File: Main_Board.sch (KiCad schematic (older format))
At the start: 64 parts, among them J1 DAC_12-bits, J2 Bias_Header, J3 Measurement_Header, Q1 Q_PNP_BCE, Q2 Q_NPN_BCE, U1 AD667, U2 LF356, U3 AD558JN

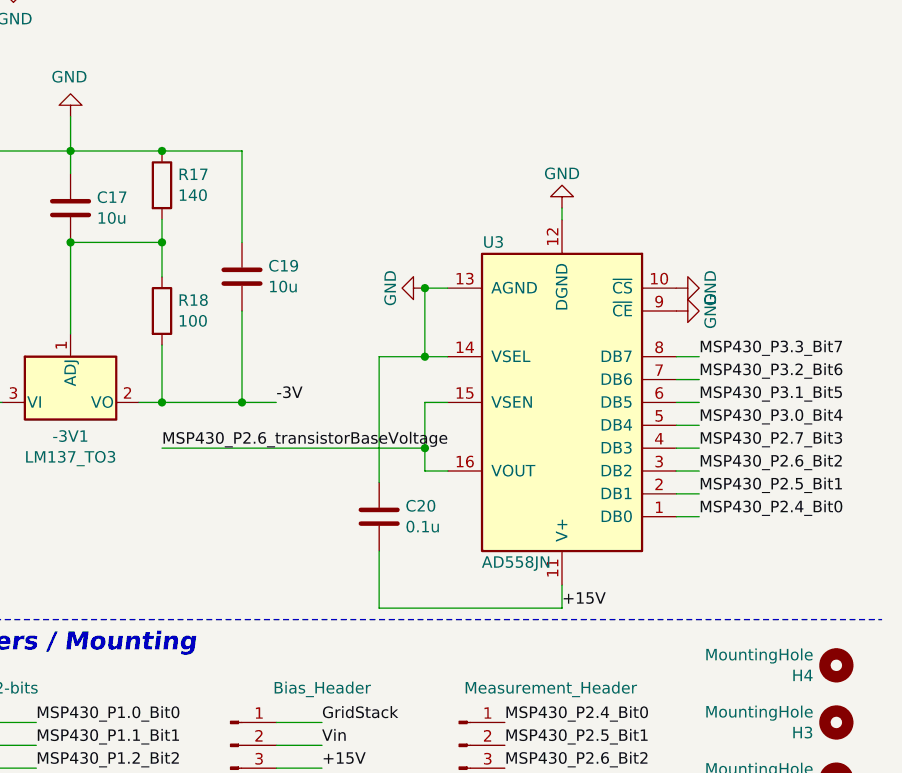
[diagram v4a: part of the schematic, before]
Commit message: Got rid of 8-bit DAC
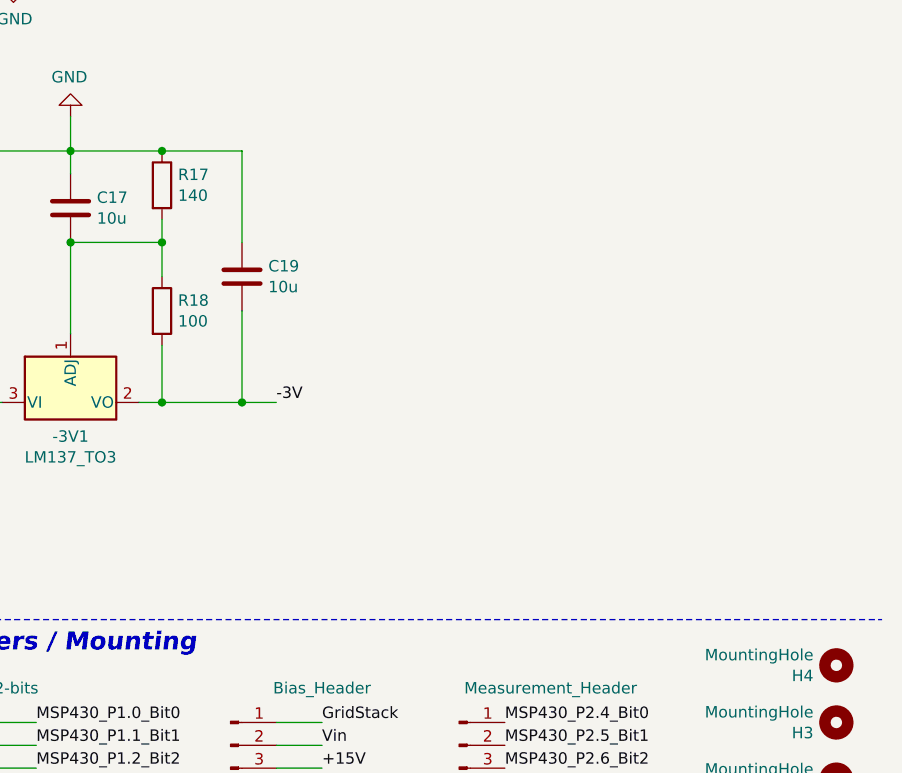
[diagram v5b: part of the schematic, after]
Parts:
- removed C20: 0.1u, Capacitor_SMD:C_0805_2012Metric, symbol Device:C
- removed U3: AD558JN, Package_DIP:DIP-16_W7.62mm_Socket, symbol Analog_DAC:AD558JN
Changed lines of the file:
@@
 	8000 1800 8000 1750
 Connection ~ 8000 1750
-Text Label 10450 3700 0    50   ~ 0
-MSP430_P3.3_Bit7
-Text Label 10450 3800 0    50   ~ 0
-MSP430_P3.2_Bit6
-Text Label 10450 3900 0    50   ~ 0
-MSP430_P3.1_Bit5
-Text Label 10450 4000 0    50   ~ 0
-MSP430_P3.0_Bit4
-Text Label 10450 4100 0    50   ~ 0
-MSP430_P2.7_Bit3
-Text Label 10450 4200 0    50   ~ 0
-MSP430_P2.6_Bit2
-Text Label 10450 4300 0    50   ~ 0
-MSP430_P2.5_Bit1
-Text Label 10450 4400 0    50   ~ 0
-MSP430_P2.4_Bit0
-Wire Wire Line
-	9850 3100 9850 3050
-Wire Wire Line
-	9850 4700 9850 4800
-Wire Wire Line
-	9350 3400 9250 3400
-Wire Wire Line
-	9350 3700 9250 3700
-Wire Wire Line
-	9350 3900 9250 3900
-Wire Wire Line
-	9350 4200 9250 4200
-Wire Wire Line
-	10350 3700 10450 3700
-Wire Wire Line
-	10350 3800 10450 3800
-Wire Wire Line
-	10350 3900 10450 3900
-Wire Wire Line
-	10350 4000 10450 4000
-Wire Wire Line
-	10350 4100 10450 4100
-Wire Wire Line
-	10350 4200 10450 4200
-Wire Wire Line
-	10350 4300 10450 4300
-Wire Wire Line
-	10350 4400 10450 4400
-$Comp
-L Analog_DAC:AD558JN U3
-U 1 1 5E52E7AD
-P 9850 3900
-F 0 "U3" H 10150 3200 50  0000 C CNN
-F 1 "AD558JN" H 10050 4600 50  0000 C CNN
-F 2 "Package_DIP:DIP-16_W7.62mm_Socket" H 9850 3900 50  0001 C CIN
-F 3 "https://www.analog.com/static/imported-files/data_sheets/AD558.pdf" H 9850 3850 50  0001 C CNN
-	1    9850 3900
-	-1   0    0    1
-$EndComp
-$Comp
-L power:GND #PWR0102
-U 1 1 5E7B08E9
-P 10350 3400
-F 0 "#PWR0102" H 10350 3150 50  0001 C CNN
-F 1 "GND" H 10350 3250 50  0000 C CNN
-F 2 "" H 10350 3400 50  0001 C CNN
-F 3 "" H 10350 3400 50  0001 C CNN
-	1    10350 3400
-	0    -1   -1   0
-$EndComp
-$Comp
-L power:GND #PWR0103
-U 1 1 5E7B1542
-P 10350 3500
-F 0 "#PWR0103" H 10350 3250 50  0001 C CNN
-F 1 "GND" H 10350 3350 50  0000 C CNN
-F 2 "" H 10350 3500 50  0001 C CNN
-F 3 "" H 10350 3500 50  0001 C CNN
-	1    10350 3500
-	0    -1   -1   0
-$EndComp
-$Comp
-L power:GND #PWR0104
-U 1 1 5E7B174D
-P 9250 3400
-F 0 "#PWR0104" H 9250 3150 50  0001 C CNN
-F 1 "GND" H 9250 3250 50  0000 C CNN
-F 2 "" H 9250 3400 50  0001 C CNN
-F 3 "" H 9250 3400 50  0001 C CNN
-	1    9250 3400
-	0    1    1    0
-$EndComp
-$Comp
-L power:GND #PWR0105
-U 1 1 5E7B21AF
-P 9850 3050
-F 0 "#PWR0105" H 9850 2800 50  0001 C CNN
-F 1 "GND" H 9850 2900 50  0000 C CNN
-F 2 "" H 9850 3050 50  0001 C CNN
-F 3 "" H 9850 3050 50  0001 C CNN
-	1    9850 3050
-	-1   0    0    1
-$EndComp
-Text Label 9850 4800 0    50   ~ 0
-+15V
 Text Label 9600 5300 0    50   ~ 0
 MSP430_P2.4_Bit0
@@
 Text Label 9600 6000 0    50   ~ 0
 MSP430_P3.3_Bit7
-Wire Wire Line
-	9250 3700 9250 3400
-Connection ~ 9250 3400
-Wire Wire Line
-	9250 3700 9050 3700
-Wire Wire Line
-	9050 4800 9850 4800
-Connection ~ 9250 3700
-$Comp
-L Device:C C20
-U 1 1 5E5EB6F5
-P 9050 4400
-F 0 "C20" H 9165 4446 50  0000 L CNN
-F 1 "0.1u" H 9165 4355 50  0000 L CNN
-F 2 "Capacitor_SMD:C_0805_2012Metric" H 9088 4250 50  0001 C CNN
-F 3 "~" H 9050 4400 50  0001 C CNN
-	1    9050 4400
-	1    0    0    -1
-$EndComp
-Wire Wire Line
-	9050 3700 9050 4250
-Wire Wire Line
-	9050 4800 9050 4550
 Text Label 9600 6400 0    50   ~ 0
 MSP430_P2.6_transistorBaseVoltage
-Text Label 8100 4100 0    50   ~ 0
-MSP430_P2.6_transistorBaseVoltage
-Wire Wire Line
-	8100 4100 9250 4100
-Wire Wire Line
-	9250 3900 9250 4100
-Connection ~ 9250 4100
-Wire Wire Line
-	9250 4100 9250 4200
 $Comp
 L Connector:Conn_01x12_Male J3

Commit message: Changing values to silk screen
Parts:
- R12: value 4.99K -> 5K
- R13: value 1.053K -> 1K
- R14: value 298 -> 300
- R16: value 3.746K -> 3.75K
- R5: value 4.12K -> 4.1K
- R6: value 3.01K -> 3K
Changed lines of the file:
@@
 P 1550 1750
 F 0 "R6" H 1620 1796 50  0000 L CNN
-F 1 "3.01K" H 1620 1705 50  0000 L CNN
+F 1 "3K" H 1620 1705 50  0000 L CNN
 F 2 "Resistor_SMD:R_0805_2012Metric" V 1480 1750 50  0001 C CNN
 F 3 "~" H 1550 1750 50  0001 C CNN
@@
 P 1550 1350
 F 0 "R5" H 1620 1396 50  0000 L CNN
-F 1 "4.12K" H 1620 1305 50  0000 L CNN
+F 1 "4.1K" H 1620 1305 50  0000 L CNN
 F 2 "Resistor_SMD:R_0805_2012Metric" V 1480 1350 50  0001 C CNN
 F 3 "~" H 1550 1350 50  0001 C CNN
@@
 P 3800 1550
 F 0 "R12" H 3870 1596 50  0000 L CNN
-F 1 "4.99K" H 3870 1505 50  0000 L CNN
+F 1 "5K" H 3870 1505 50  0000 L CNN
 F 2 "Resistor_SMD:R_0805_2012Metric" V 3730 1550 50  0001 C CNN
 F 3 "~" H 3800 1550 50  0001 C CNN
@@
 P 5350 1800
 F 0 "R13" H 5420 1846 50  0000 L CNN
-F 1 "1.053K" H 5420 1755 50  0000 L CNN
+F 1 "1K" H 5420 1755 50  0000 L CNN
 F 2 "Resistor_SMD:R_0805_2012Metric" V 5280 1800 50  0001 C CNN
 F 3 "~" H 5350 1800 50  0001 C CNN
@@
 Vin
 $Comp
-L Device:R R16
-U 1 1 5DCC6D68
-P 6550 1100
-F 0 "R16" H 6620 1146 50  0000 L CNN
-F 1 "3.746K" H 6620 1055 50  0000 L CNN
-F 2 "Resistor_SMD:R_0805_2012Metric" V 6480 1100 50  0001 C CNN
-F 3 "~" H 6550 1100 50  0001 C CNN
-	1    6550 1100
-	1    0    0    -1
-$EndComp
-$Comp
 L Device:R R19
 U 1 1 5DCC8357
@@
 P 5950 2950
 F 0 "R14" H 6020 2996 50  0000 L CNN
-F 1 "298" H 6020 2905 50  0000 L CNN
+F 1 "300" H 6020 2905 50  0000 L CNN
 F 2 "Resistor_SMD:R_0805_2012Metric" V 5880 2950 50  0001 C CNN
 F 3 "~" H 5950 2950 50  0001 C CNN
@@
 NoConn ~ 8800 6200
 NoConn ~ 8800 6300
+$Comp
+L Device:R R16
+U 1 1 5DCC6D68
+P 6550 1100
+F 0 "R16" H 6620 1146 50  0000 L CNN
+F 1 "3.75K" H 6620 1055 50  0000 L CNN
+F 2 "Resistor_SMD:R_0805_2012Metric" V 6480 1100 50  0001 C CNN
+F 3 "~" H 6550 1100 50  0001 C CNN
+	1    6550 1100
+	1    0    0    -1
+$EndComp
 $EndSCHEMATC

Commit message: -200 Return
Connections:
- net -200_Return: now reaches J2.11 (Pin_11)
- no-connect marks 5 -> 4
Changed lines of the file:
@@
 -200V
 NoConn ~ 8800 6200
-NoConn ~ 8800 6300
 $Comp
 L Device:R R16
@@
 	1    0    0    -1
 $EndComp
+Text Label 8800 6300 0    50   ~ 0
+-200_Return
 $EndSCHEMATC

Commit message: update label
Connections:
- net MSP430_P2.5_filamentCurrent renamed MSP430_P2.5_emitterCurrent
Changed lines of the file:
@@
 $EndComp
 Text Label 9600 6200 0    50   ~ 0
-MSP430_P2.5_filamentCurrent
+MSP430_P2.5_emitterCurrent
 Text Label 9600 6300 0    50   ~ 0
 MSP430_P2.7_cemMeasure
